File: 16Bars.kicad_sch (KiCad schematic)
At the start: 24 parts, among them J1 3.5mm_Mono_Switched, J2 Conn_02x05_Odd_Even, J3 Conn_01x04, J4 3.5mm_Mono_Switched, J5 3.5mm_Mono_Switched, J6 3.5mm_Mono_Switched, SW1 SW_Push_LED_Thonk_Low_Profile, SW3 SW_SPDT-EG1249

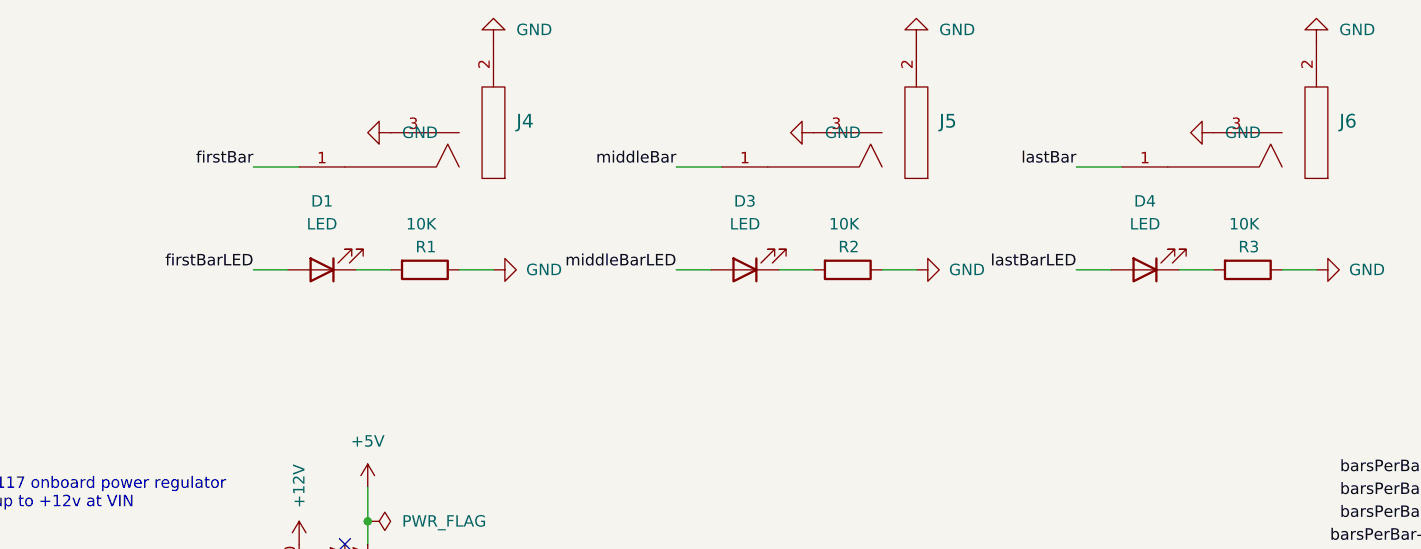
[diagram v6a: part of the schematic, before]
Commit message: Generate 3.0 Fabrication
Added JLC bom python script.
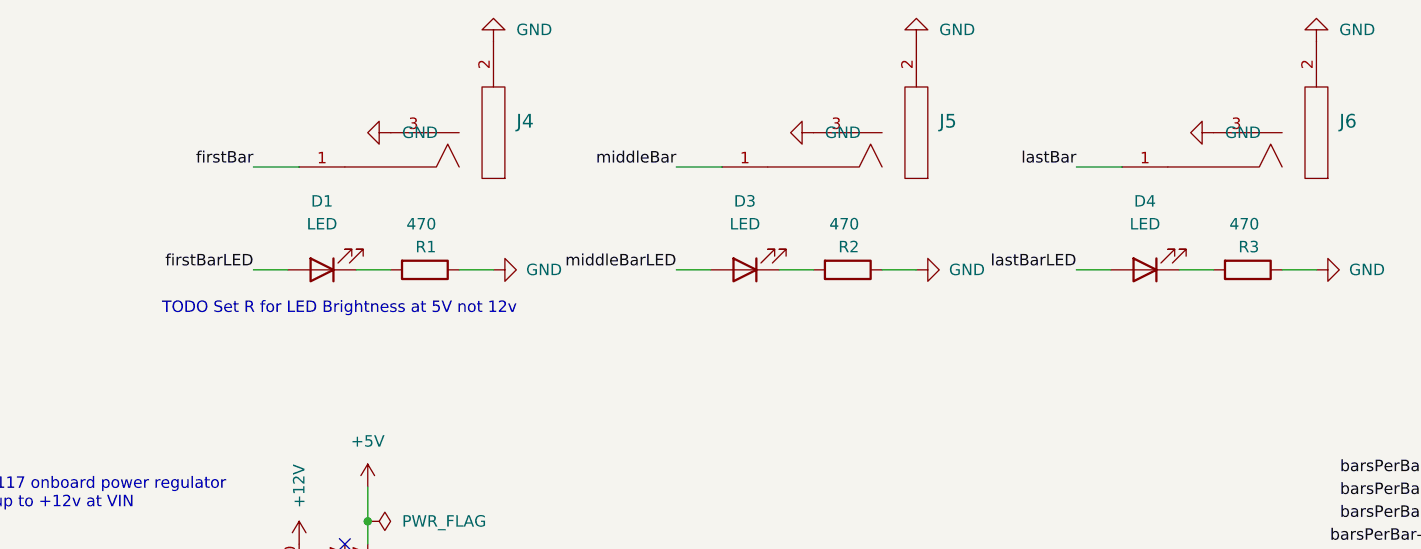
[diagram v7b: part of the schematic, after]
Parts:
- R1, R2, R3: value 10K -> 470; LCSC C4109 -> C25117
- R5: LCSC C25792 -> C25117
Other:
- note added: "TODO Set R for LED Brightness at 5V not 12v"
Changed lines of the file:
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@@
+    (effects (font (size 1.27 1.27)) (justify left bottom))
+  )
+  (text "TODO Set R for LED Brightness at 5V not 12v" (at 85.09 52.07 0)
     (effects (font (size 1.27 1.27)) (justify left bottom))
   )
@@
   (symbol (lib_id "power:GND") (at 203.2 104.14 270) (unit 1)
     (in_bom yes) (on_board yes)
-    (property "Reference" "#PWR?" (id 0) (at 196.85 104.14 0)
+    (property "Reference" "#PWR0104" (id 0) (at 196.85 104.14 0)
       (effects (font (size 1.27 1.27)) hide)
     )
@@
       (effects (font (size 1.27 1.27)) (justify right))
     )
-    (property "Value" "10K" (id 1) (at 115.57 41.9101 90)
+    (property "Value" "470" (id 1) (at 115.57 41.9101 90)
       (effects (font (size 1.27 1.27)) (justify right))
     )
@@
       (effects (font (size 1.27 1.27)) hide)
     )
-    (property "LCSC" "C4109" (id 4) (at 114.3 46.99 90)
+    (property "LCSC" "C25117" (id 4) (at 114.3 46.99 90)
       (effects (font (size 1.27 1.27)) hide)
     )
@@
       (effects (font (size 1.27 1.27)) (justify right))
     )
-    (property "Value" "10K" (id 1) (at 207.01 41.9101 90)
+    (property "Value" "470" (id 1) (at 207.01 41.9101 90)
       (effects (font (size 1.27 1.27)) (justify right))
     )
@@
       (effects (font (size 1.27 1.27)) hide)
     )
-    (property "LCSC" "C4109" (id 4) (at 205.74 46.99 90)
+    (property "LCSC" "C25117" (id 4) (at 205.74 46.99 90)
       (effects (font (size 1.27 1.27)) hide)
     )
@@
   (symbol (lib_id "power:+5V") (at 203.2 97.79 90) (unit 1)
     (in_bom yes) (on_board yes)
-    (property "Reference" "#PWR?" (id 0) (at 207.01 97.79 0)
+    (property "Reference" "#PWR0103" (id 0) (at 207.01 97.79 0)
       (effects (font (size 1.27 1.27)) hide)
     )
@@
       (effects (font (size 1.27 1.27)) hide)
     )
-    (property "LCSC" "C25792" (id 4) (at 198.12 133.35 90)
+    (property "LCSC" "C25117" (id 4) (at 198.12 133.35 90)
       (effects (font (size 1.27 1.27)) hide)
     )
@@
       (effects (font (size 1.27 1.27)) (justify right))
     )
-    (property "Value" "10K" (id 1) (at 162.56 41.9101 90)
+    (property "Value" "470" (id 1) (at 162.56 41.9101 90)
       (effects (font (size 1.27 1.27)) (justify right))
     )
@@
       (effects (font (size 1.27 1.27)) hide)
     )
-    (property "LCSC" "C4109" (id 4) (at 161.29 46.99 90)
+    (property "LCSC" "C25117" (id 4) (at 161.29 46.99 90)
       (effects (font (size 1.27 1.27)) hide)
     )
@@
       (reference "#PWR0102") (unit 1) (value "+5V") (footprint "")
     )
+    (path "/27e0667d-ee51-4a7a-bccb-99809e915c8d"
+      (reference "#PWR0103") (unit 1) (value "+5V") (footprint "")
+    )
+    (path "/1a4d2f98-eb29-411d-b00e-421a80da643d"
+      (reference "#PWR0104") (unit 1) (value "GND") (footprint "")
+    )
     (path "/865dfb96-b22c-42c0-be06-07959f919c05"
       (reference "#PWR0110") (unit 1) (value "+12V") (footprint "")
@@
       (reference "#PWR0113") (unit 1) (value "GND") (footprint "")
     )
-    (path "/1a4d2f98-eb29-411d-b00e-421a80da643d"
-      (reference "#PWR?") (unit 1) (value "GND") (footprint "")
-    )
-    (path "/27e0667d-ee51-4a7a-bccb-99809e915c8d"
-      (reference "#PWR?") (unit 1) (value "+5V") (footprint "")
-    )
     (path "/dae1ea8a-32da-4426-8f99-becaad375e16"
       (reference "A1") (unit 1) (value "Arduino_Nano_v3.x") (footprint "Module:Arduino_Nano")
@@
     )
     (path "/1b512e00-f29f-4fe5-bc1c-e76b42eb948f"
-      (reference "R1") (unit 1) (value "10K") (footprint "Resistor_SMD:R_0402_1005Metric")
+      (reference "R1") (unit 1) (value "470") (footprint "Resistor_SMD:R_0402_1005Metric")
     )
     (path "/b9c8222a-e057-41d6-b54c-b389ff44d23b"
-      (reference "R2") (unit 1) (value "10K") (footprint "Resistor_SMD:R_0402_1005Metric")
+      (reference "R2") (unit 1) (value "470") (footprint "Resistor_SMD:R_0402_1005Metric")
     )
     (path "/22c57990-6b78-4f18-8ec6-f1540678b43e"
-      (reference "R3") (unit 1) (value "10K") (footprint "Resistor_SMD:R_0402_1005Metric")
+      (reference "R3") (unit 1) (value "470") (footprint "Resistor_SMD:R_0402_1005Metric")
     )
     (path "/b7a58442-8471-47d1-8f65-f9b0cc04ffba"

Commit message: v3.1
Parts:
- added J7: SevenSegmentGround, 4ms_Connector:Pins_1x03_2.54mm_TH_AudioInsRGndL, symbol 4ms_Connector:Conn_01x03
- J3: value Conn_01x04 -> SevenSegmentHeader; footprint 4ms_Connector:Pins_1x04_2.54mm_TH_SWD -> 4ms_Connector:Pins_1x03_2.54mm_TH_AudioInsRGndL; symbol 4ms_Connector:Conn_01x04 -> 4ms_Connector:Conn_01x03; Part Number 1-0401FBV0T -> 1-0301FBV0T; Specifications HEADER 1x4 MALE PINS 0.100” 180deg -> HEADER 1x3 MALE PINS 0.100” 180deg
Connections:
- net GND: now also J7.1 (Pin_1), J7.2 (Pin_2), J7.3 (Pin_3); no longer J3.2 (Pin_2)
- net RESET: now also J3.2 (Pin_2); no longer J3.4 (Pin_4)
- net barsPerPhrase: now also A1.23 (A4); no longer A1.9 (D6)
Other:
- note removed: "SevenSegment Headers"
